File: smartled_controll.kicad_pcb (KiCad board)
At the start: 2 copper layers, 61.2 x 43.7 mm, 95 parts, among them J1 Conn_01x04, J2 Conn_01x02, SW1 SW_Push, U1 OC5028B, U2 MAX485E, U3 PY32F003F1xUx, U4 OC5864, U5 need chooice, U6 OC5028B, U7 need chooice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

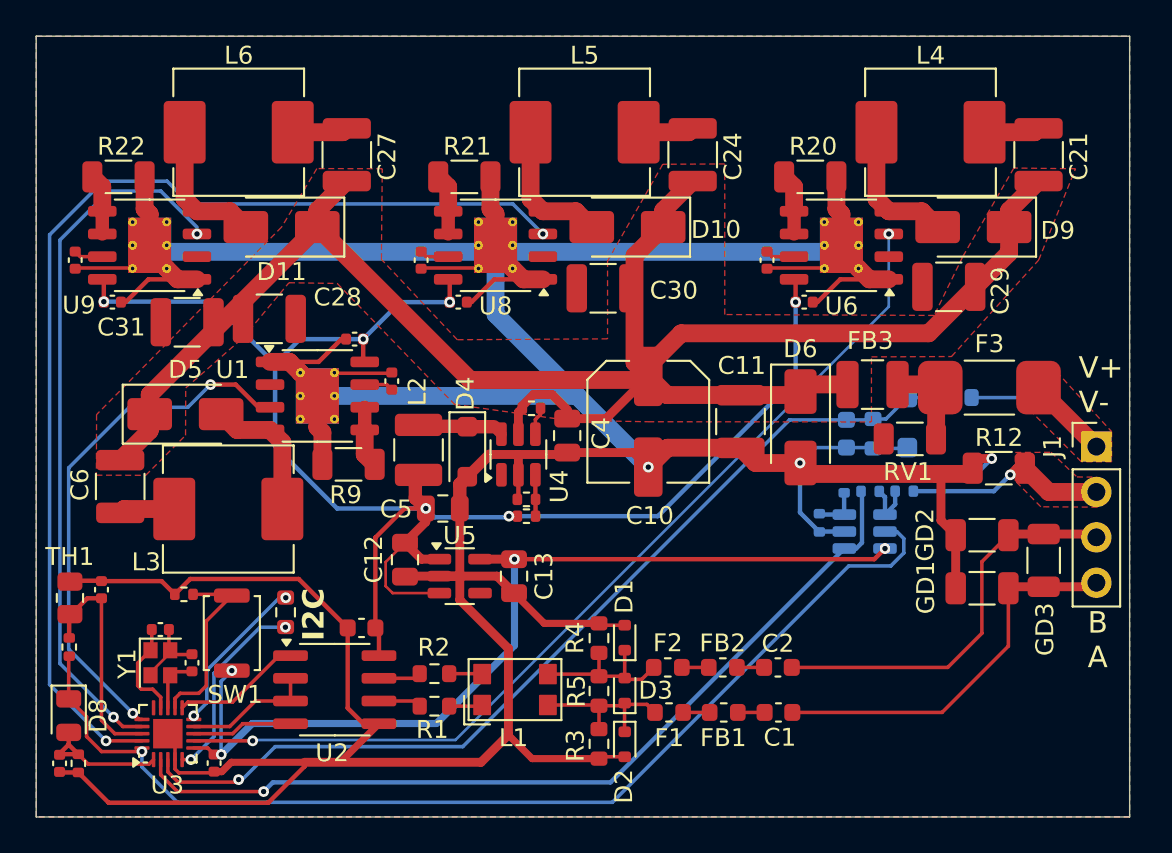
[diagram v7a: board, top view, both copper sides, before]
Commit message: 选择3.3V LDO和电流采样运放的型号
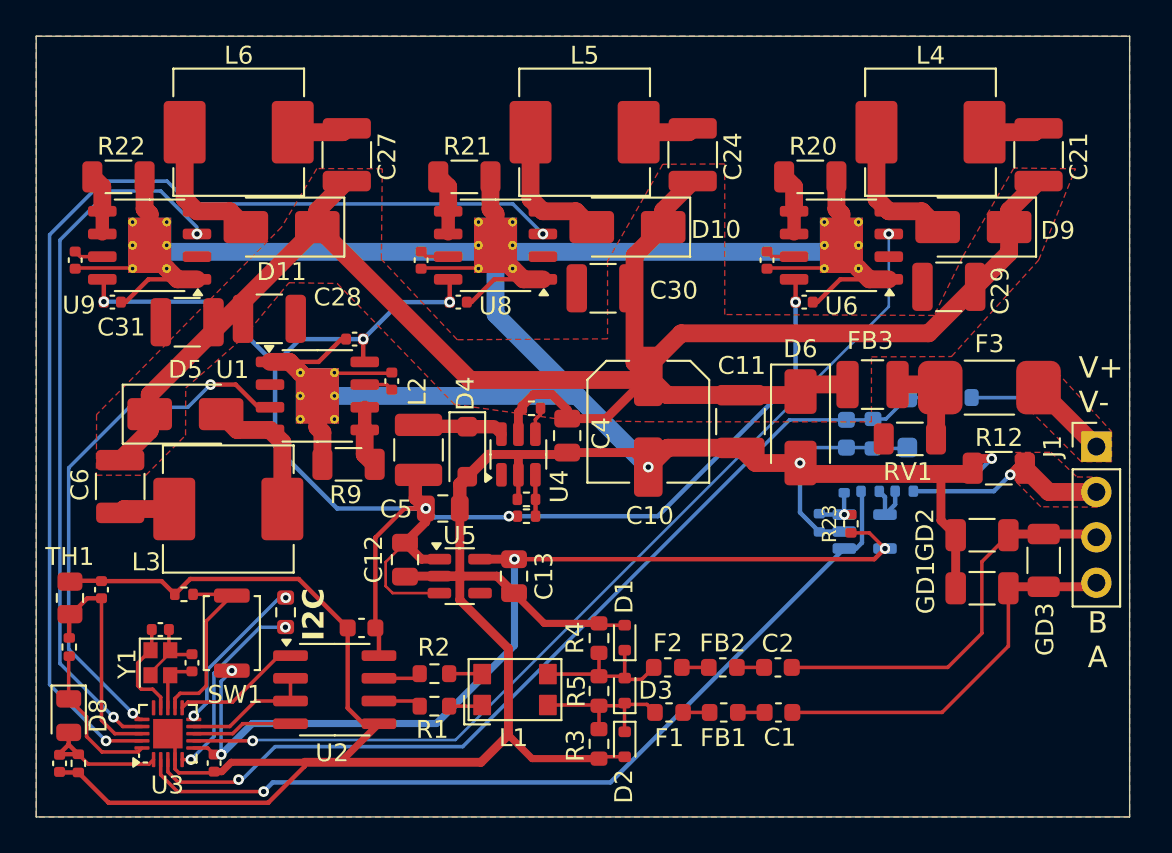
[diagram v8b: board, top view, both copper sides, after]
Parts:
- added R23: R, Resistor_SMD:R_0402_1005Metric, F.Cu at (178.0, 79.3)
- U5: value need chooice -> SGM2033-3.3
- U7: value need chooice -> GS8521; footprint Package_TO_SOT_SMD:SOT-23-6 -> Package_TO_SOT_SMD:TSOT-23-5
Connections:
- U7 pad 5: /SampEn -> +3.3V
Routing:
- net /SampEn: track 60.7 -> 8.47 mm, vias 1 -> 0
- net +3.3V: track 53.3 -> 55.6 mm
- net Net-(U7-+): track 2.64 -> 3.01 mm, vias 0 -> 1
